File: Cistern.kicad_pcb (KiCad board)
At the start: 2 copper layers, 51 x 83 mm, 14 parts, among them J2 Gauge Stepper, J3 Power Connector, Q1 IRF9540N, SW1 WiFi reset switch, SW2 Water Sensor, U1 ULN2003A, U3 Boost Converter (5->20 V)

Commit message: Changing schematic to fit parts and starting PCB design
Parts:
- D1: footprint LED_THT:LED_D4.0mm -> LED_THT:LED_D5.0mm
- Q1: value IRF9540N -> BD244C
- R1: value 250 -> 150
- R2: value 200k -> 68
- R4: value 160 -> 150
- moved SW1 85.8 mm to (112.5, 22.6), turned to 180 degrees
- moved U3 63.6 mm to (76.2, 99.1)
- moved J2 56.8 mm to (63.5, 94.0), turned to 180 degrees
- moved U1 36.4 mm to (66.0, 78.7), turned to -90 degrees
- moved R2 32.6 mm to (71.1, 96.5), turned to 90 degrees
- moved D2 26.4 mm to (88.9, 48.3), turned to -90 degrees
- moved D1 22.1 mm to (33.0, 88.9)
- moved Q1 19.1 mm to (71.1, 78.7), turned to -90 degrees
- moved D3 18.1 mm to (81.3, 48.3), turned to 180 degrees
- moved R1 14.3 mm to (81.3, 53.3), turned to 180 degrees
- moved J3 13.7 mm to (88.9, 38.1), turned to -90 degrees
- moved R4 2.39 mm to (45.7, 91.4), turned to -90 degrees
- moved SW2 1.30 mm to (88.9, 27.9), turned to -90 degrees
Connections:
- Q1 pad 1: Net-(Q1-G) -> Net-(Q1-B)
- R2 pad 1: +5V -> Net-(Q1-B)
- R2 pad 2: Net-(Q1-G) -> Net-(U1-O1)
- U1 pad 1: Net-(MCU1-GPIO27) -> Net-(MCU1-GPIO35)
- U1 pad 10: Net-(D1-K) -> unconnected-(U1-O7-Pad10)
- U1 pad 11: Net-(Q1-G) -> Net-(D1-K)
- U1 pad 12: unconnected-(U1-O5-Pad12) -> Net-(J2-Pin_4)
- U1 pad 13: Net-(J2-Pin_4) -> Net-(J2-Pin_3)
- U1 pad 14: Net-(J2-Pin_3) -> Net-(J2-Pin_2)
- U1 pad 15: Net-(J2-Pin_2) -> Net-(J2-Pin_1)
- U1 pad 16: Net-(J2-Pin_1) -> Net-(U1-O1)
- U1 pad 2: Net-(MCU1-GPIO26) -> Net-(MCU1-GPIO32)
- U1 pad 3: Net-(MCU1-GPIO25) -> Net-(MCU1-GPIO33)
- U1 pad 4: Net-(MCU1-GPIO33) -> Net-(MCU1-GPIO25)
- U1 pad 5: unconnected-(U1-I5-Pad5) -> Net-(MCU1-GPIO26)
- U1 pad 6: Net-(MCU1-GPIO32) -> Net-(MCU1-GPIO27)
- U1 pad 7: Net-(MCU1-GPIO35) -> unconnected-(U1-I7-Pad7)
- U1 pad 9: GND -> +5V
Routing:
- net GND: track 0.00 -> 114.3 mm
- net Net-(MCU1-GPIO15): track 0.00 -> 43.2 mm
- net +5V: track 0.00 -> 25.4 mm
- net Net-(MCU1-GPIO4): track 0.00 -> 20.3 mm
- net Net-(D2-A): track 0.00 -> 18.0 mm
- net Net-(D2-K): track 0.00 -> 12.7 mm
- removed copper zone on B.Cu, net (none)
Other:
- board size 51 x 83 mm -> 55.5 x 79.6 mm

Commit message: Working on board layout
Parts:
- added BZ1: Buzzer, Cistern:AZDelivery_KY-012_Buzzer, F.Cu at (48.3, 78.7)
- D2, SW2: footprint TerminalBlock:TerminalBlock_bornier-2_P5.08mm -> Connector_PinHeader_2.54mm:PinHeader_1x02_P2.54mm_Vertical
- moved SW1 80.0 mm to (43.8, 63.5), turned to 90 degrees
- moved J3 74.7 mm to (45.7, 99.1), turned to 0 degrees
- moved D2 52.4 mm to (68.6, 96.5), turned to 90 degrees
- moved D3 48.8 mm to (50.8, 86.4)
- moved R1 48.8 mm to (50.8, 91.4)
- moved U3 43.8 mm to (94.0, 59.1), turned to -90 degrees
- moved MCU1 27.0 mm to (48.3, 50.8), turned to 90 degrees
- moved SW2 25.5 mm to (91.4, 53.3)
- moved D1 25.5 mm to (58.4, 86.4)
- moved J2 23.4 mm to (68.6, 71.1)
- moved U1 23.4 mm to (71.1, 55.9)
- moved Q1 13.7 mm to (66.0, 91.4), turned to 90 degrees
- moved R4 12.7 mm to (53.3, 81.3), turned to 90 degrees
- moved R2 5.08 mm to (71.1, 91.4)
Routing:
- net +5V: track 25.4 -> 129.5 mm
- net Net-(Q1-C): track 0.00 -> 57.8 mm
- net Net-(BZ1--): track 0.00 -> 20.3 mm
- net Net-(U1-O1): track 0.00 -> 20.3 mm
- net GND: track 114.3 -> 129.4 mm
- net Net-(MCU1-GPIO4): track 20.3 -> 6.50 mm
- net Net-(D2-K): track 12.7 -> 22.9 mm
- net Net-(J2-Pin_4): track 0.00 -> 7.62 mm
- net Net-(J2-Pin_3): track 0.00 -> 7.62 mm
- net Net-(J2-Pin_2): track 0.00 -> 7.62 mm
- net Net-(J2-Pin_1): track 0.00 -> 7.62 mm
- net Net-(D2-A): track 18.0 -> 25.4 mm
- net Net-(Q1-B): track 0.00 -> 5.08 mm
- net Net-(MCU1-GPIO15): track 43.2 -> 40.6 mm

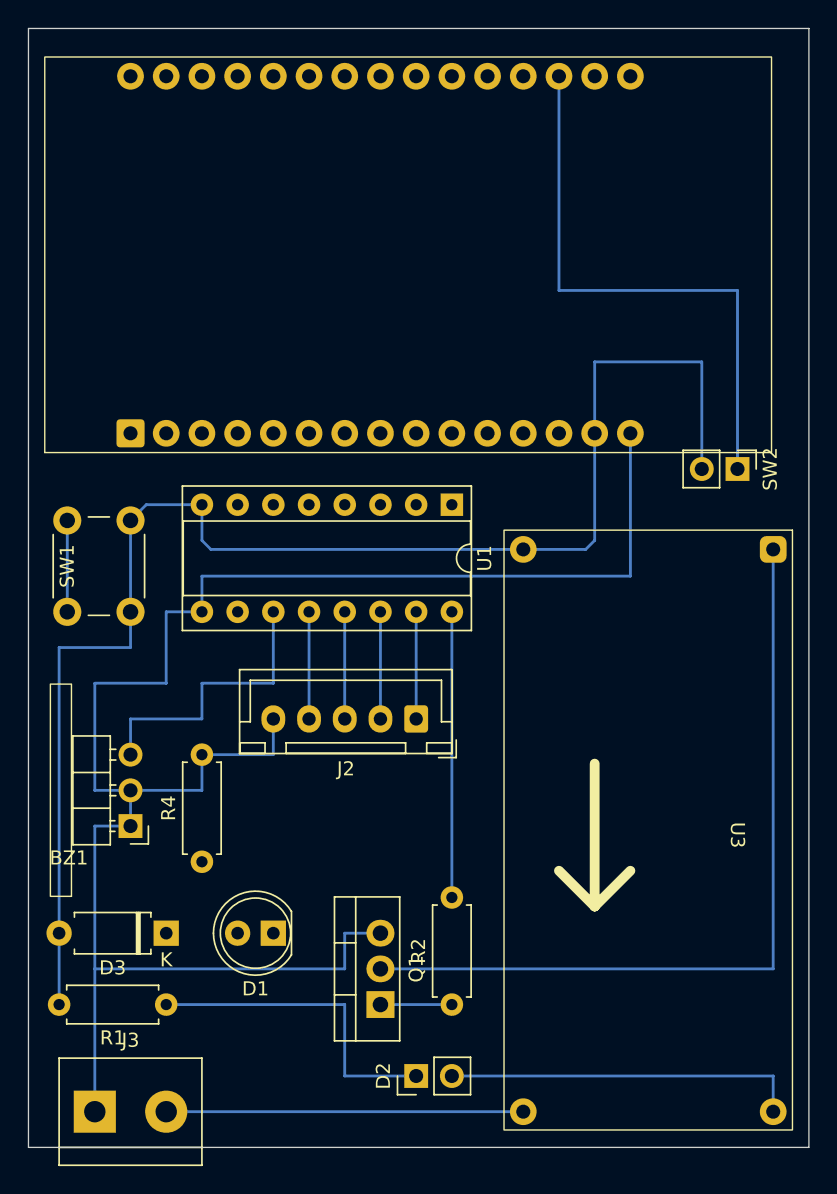
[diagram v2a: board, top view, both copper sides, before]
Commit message: Finishing hole-grid ready PCB design
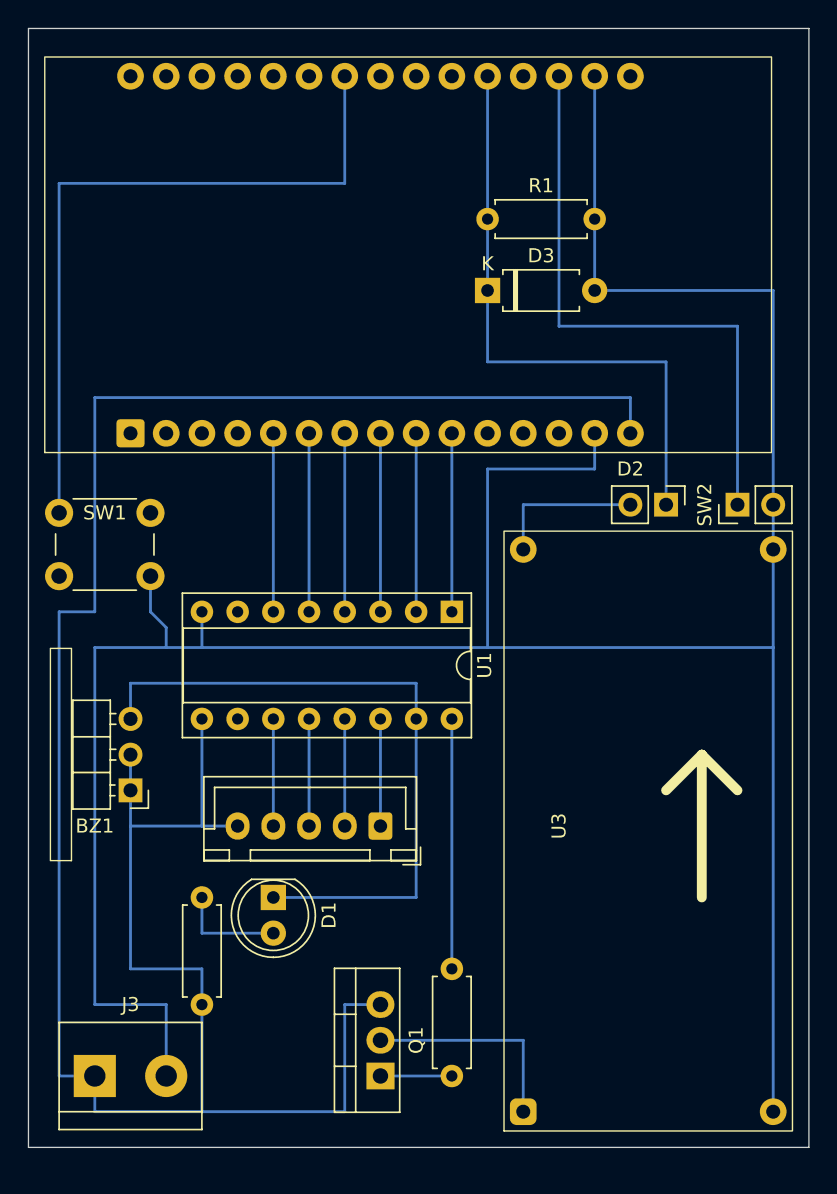
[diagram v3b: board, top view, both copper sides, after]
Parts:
- SW1: value WiFi reset switch -> WiFi reset
- moved R1 60.4 mm to (73.7, 35.6), turned to 0 degrees
- moved D3 51.1 mm to (73.7, 40.6), turned to 0 degrees
- moved D2 44.4 mm to (86.4, 55.9), turned to -90 degrees
- moved U3 43.8 mm to (76.2, 99.1), turned to 90 degrees
- moved J2 8.03 mm to (66.0, 78.7)
- moved U1 7.62 mm to (71.1, 63.5)
- moved SW1 7.06 mm to (43.2, 56.5), turned to 0 degrees
- moved Q1 5.08 mm to (66.0, 96.5)
- moved R2 5.08 mm to (71.1, 96.5)
- moved D1 2.54 mm to (58.4, 83.8), turned to -90 degrees
- moved J3 2.54 mm to (45.7, 96.5)
- moved SW2 2.54 mm to (91.4, 55.9), turned to 90 degrees
- moved BZ1 2.54 mm to (48.3, 76.2)
- moved R4 2.54 mm to (53.3, 83.8), turned to -90 degrees
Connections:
- MCU1 pad 22: Net-(D2-K) -> Net-(MCU1-GPIO18)
- MCU1 pad 26: Net-(MCU1-GPIO4) -> Net-(D2-K)
- SW1 pad 1: Net-(MCU1-GPIO4) -> Net-(MCU1-GPIO18)
- U1 pad 1: Net-(MCU1-GPIO35) -> Net-(MCU1-GPIO27)
- U1 pad 11: Net-(BZ1--) -> Net-(J2-Pin_4)
- U1 pad 12: Net-(J2-Pin_4) -> Net-(J2-Pin_3)
- U1 pad 13: Net-(J2-Pin_3) -> Net-(J2-Pin_2)
- U1 pad 14: Net-(J2-Pin_2) -> Net-(J2-Pin_1)
- U1 pad 15: Net-(J2-Pin_1) -> Net-(BZ1--)
- U1 pad 2: Net-(MCU1-GPIO32) -> Net-(MCU1-GPIO26)
- U1 pad 3: Net-(MCU1-GPIO33) -> Net-(MCU1-GPIO25)
- U1 pad 4: Net-(MCU1-GPIO25) -> Net-(MCU1-GPIO33)
- U1 pad 5: Net-(MCU1-GPIO26) -> Net-(MCU1-GPIO32)
- U1 pad 6: Net-(MCU1-GPIO27) -> Net-(MCU1-GPIO35)
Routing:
- net GND: track 129.4 -> 201.1 mm
- net Net-(MCU1-GPIO18): track 0.00 -> 51.4 mm
- net Net-(Q1-C): track 57.8 -> 15.2 mm
- net +5V: track 129.5 -> 170.2 mm
- net Net-(BZ1--): track 20.3 -> 48.3 mm
- net Net-(D2-K): track 22.9 -> 43.2 mm
- net Net-(D2-A): track 25.4 -> 10.8 mm
- net Net-(MCU1-GPIO35): track 0.00 -> 12.7 mm
- net Net-(MCU1-GPIO33): track 0.00 -> 12.7 mm
- net Net-(MCU1-GPIO32): track 0.00 -> 12.7 mm
- net Net-(MCU1-GPIO27): track 0.00 -> 12.7 mm
- net Net-(MCU1-GPIO26): track 0.00 -> 12.7 mm
- net Net-(MCU1-GPIO25): track 0.00 -> 12.7 mm
- net Net-(D1-A): track 0.00 -> 7.62 mm
- net Net-(MCU1-GPIO4): track 6.50 -> 0.00 mm
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
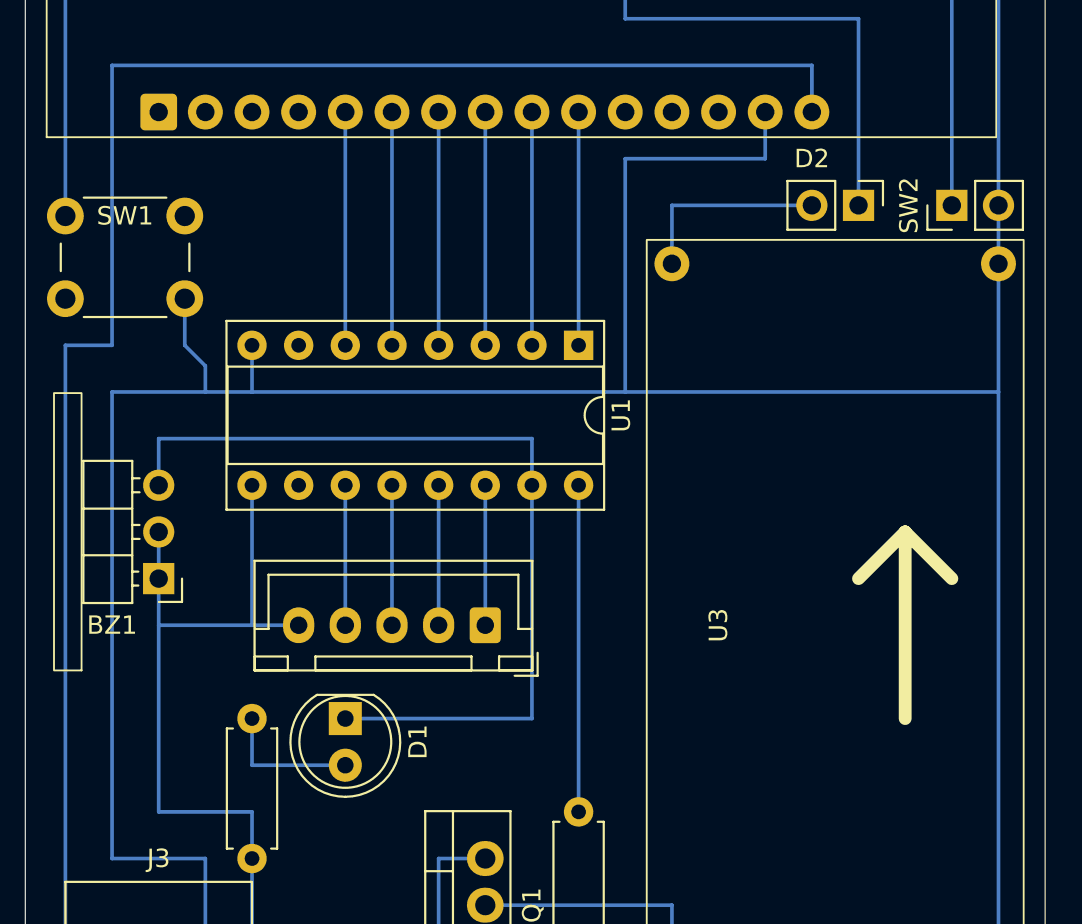
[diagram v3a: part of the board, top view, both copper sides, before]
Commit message: Small improvement to buzzer clearance
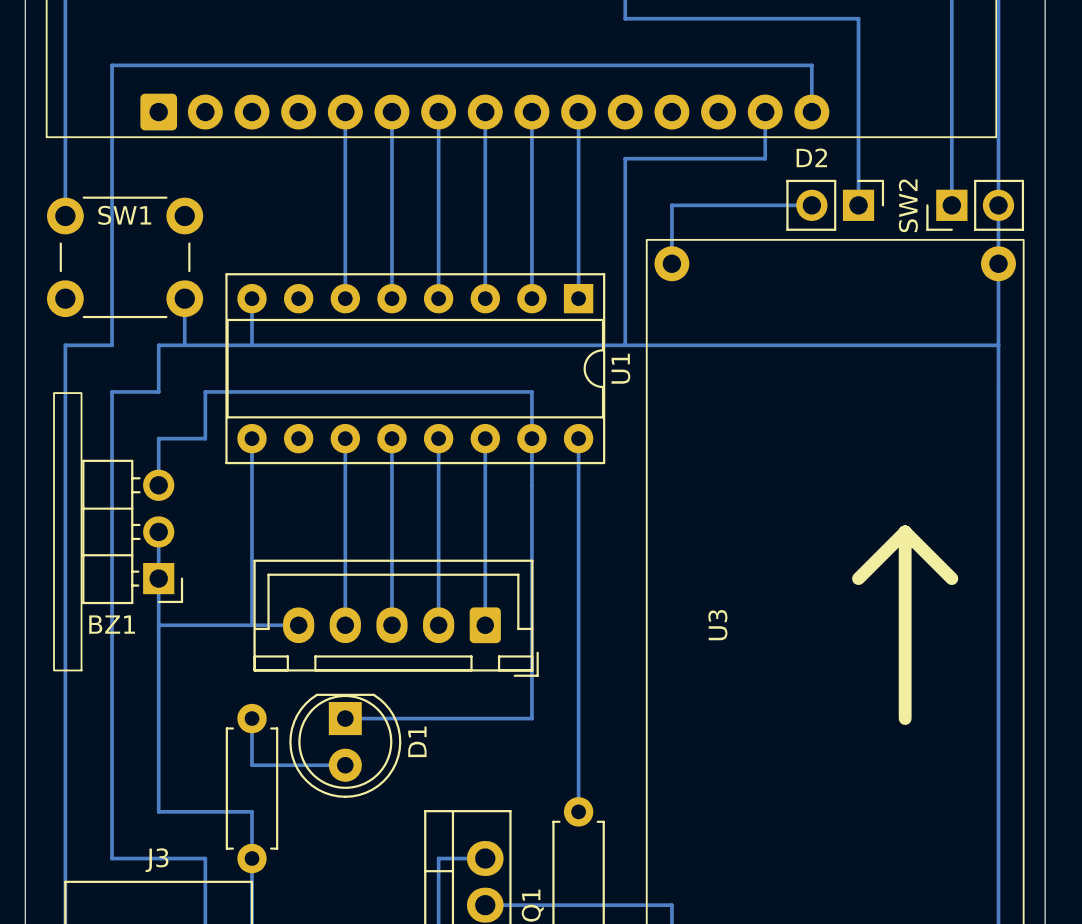
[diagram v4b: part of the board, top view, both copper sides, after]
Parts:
- moved U1 2.54 mm to (71.1, 61.0)
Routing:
- net Net-(BZ1--): track 48.3 -> 53.3 mm
- net GND: track 201.1 -> 198.1 mm
- net Net-(U1-O1): track 17.8 -> 20.3 mm
- net Net-(J2-Pin_4): track 7.62 -> 10.2 mm
- net Net-(J2-Pin_3): track 7.62 -> 10.2 mm
- net Net-(J2-Pin_2): track 7.62 -> 10.2 mm
- net Net-(J2-Pin_1): track 7.62 -> 10.2 mm
- net Net-(MCU1-GPIO35): track 12.7 -> 10.2 mm
- net Net-(MCU1-GPIO33): track 12.7 -> 10.2 mm
- net Net-(MCU1-GPIO32): track 12.7 -> 10.2 mm
- net Net-(MCU1-GPIO27): track 12.7 -> 10.2 mm
- net Net-(MCU1-GPIO26): track 12.7 -> 10.2 mm
- net Net-(MCU1-GPIO25): track 12.7 -> 10.2 mm
- net +5V: track 170.2 -> 172.7 mm
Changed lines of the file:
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@@
 		)
 		(fp_text user "${REFERENCE}"
-			(at 0 1.27 360)
+			(at 0 1.27 0)
 			(layer "F.Fab")
 			(effects
@@
 		(tags "Diode A-405 series Axial Horizontal pin pitch 7.62mm  length 5.2mm diameter 2.7mm")
 		(property "Reference" "D3"
-			(at 3.81 -2.47 360)
+			(at 3.81 -2.47 0)
 			(layer "F.SilkS")
 			(effects
@@
 		)
 		(property "Value" "3V"
-			(at 3.81 2.47 360)
+			(at 3.81 2.47 0)
 			(layer "F.Fab")
 			(effects
@@
 		)
 		(fp_text user "K"
-			(at 0 -1.9 360)
+			(at 0 -1.9 0)
 			(layer "F.SilkS")
 			(effects
@@
 		)
 		(fp_text user "${REFERENCE}"
-			(at 4.2 0 360)
+			(at 4.2 0 0)
 			(layer "F.Fab")
 			(effects
@@
 		)
 		(fp_text user "K"
-			(at 0 -1.9 360)
+			(at 0 -1.9 0)
 			(layer "F.Fab")
 			(effects
@@
 		)
 		(fp_text user "${REFERENCE}"
-			(at 0 1.27 360)
+			(at 0 1.27 0)
 			(layer "F.Fab")
 			(effects
@@
 		(tags "Resistor Axial_DIN0207 series Axial Horizontal pin pitch 7.62mm 0.25W = 1/4W length 6.3mm diameter 2.5mm")
 		(property "Reference" "R1"
-			(at 3.81 -2.37 360)
+			(at 3.81 -2.37 0)
 			(layer "F.SilkS")
 			(effects
@@
 		)
 		(property "Value" "150"
-			(at 3.81 2.37 360)
+			(at 3.81 2.37 0)
 			(layer "F.Fab")
 			(effects
@@
 		)
 		(fp_text user "${REFERENCE}"
-			(at 3.81 0 360)
+			(at 3.81 0 0)
 			(layer "F.Fab")
 			(effects
@@
 		(tags "terminal block bornier2")
 		(property "Reference" "J3"
-			(at 2.54 -5.08 360)
+			(at 2.54 -5.08 0)
 			(layer "F.SilkS")
 			(effects
@@
 		)
 		(property "Value" "Power Connector"
-			(at 2.54 3.81 360)
+			(at 2.54 3.81 0)
 			(layer "F.Fab")
 			(effects
@@
 		)
 		(fp_text user "${REFERENCE}"
-			(at 2.54 0 360)
+			(at 2.54 0 0)
 			(layer "F.Fab")
 			(effects
@@
 		(tags "tact sw push 6mm")
 		(property "Reference" "SW1"
-			(at 3.25 0 360)
+			(at 3.25 0 0)
 			(layer "F.SilkS")
 			(effects
@@
 		)
 		(fp_text user "${REFERENCE}"
-			(at 3.25 2.25 360)
+			(at 3.25 2.25 0)
 			(layer "F.Fab")
 			(effects
@@
 	(footprint "Package_DIP:DIP-16_W7.62mm_Socket"
 		(layer "F.Cu")
-		(at 71.12 63.5 -90)
+		(at 71.12 60.96 -90)
 		(descr "16-lead though-hole mounted DIP package, row spacing 7.62 mm (300 mils), Socket")
 		(tags "THT DIP DIL PDIP 2.54mm 7.62mm 300mil Socket")
@@
 	)
 	(segment
-		(start 53.34 78.74)
-		(end 53.34 71.12)
-		(width 0.2)
-		(layer "B.Cu")
-		(net 1)
-	)
-	(segment
 		(start 45.72 63.5)
 		(end 45.72 48.26)
@@
 	)
 	(segment
+		(start 53.34 68.58)
+		(end 53.34 78.74)
+		(width 0.2)
+		(layer "B.Cu")
+		(net 1)
+	)
+	(segment
 		(start 43.18 63.5)
 		(end 45.72 63.5)
@@
 	)
 	(segment
+		(start 50.8 66.04)
+		(end 68.58 66.04)
+		(width 0.2)
+		(layer "B.Cu")
+		(net 2)
+	)
+	(segment
 		(start 68.58 68.58)
 		(end 68.58 71.12)
@@
 	)
 	(segment
+		(start 68.58 66.04)
+		(end 68.58 68.58)
+		(width 0.2)
+		(layer "B.Cu")
+		(net 2)
+	)
+	(segment
 		(start 58.42 83.82)
 		(end 68.58 83.82)
@@
 	)
 	(segment
+		(start 50.8 68.58)
+		(end 50.8 66.04)
+		(width 0.2)
+		(layer "B.Cu")
+		(net 2)
+	)
+	(segment
 		(start 48.26 71.12)
 		(end 48.26 68.58)
@@
 	(segment
 		(start 48.26 68.58)
-		(end 68.58 68.58)
+		(end 50.8 68.58)
 		(width 0.2)
 		(layer "B.Cu")
@@
 	)
 	(segment
-		(start 50.8 66.04)
-		(end 53.34 66.04)
+		(start 50.8 91.44)
+		(end 45.72 91.44)
+		(width 0.2)
+		(layer "B.Cu")
+		(net 6)
+	)
+	(segment
+		(start 73.66 53.34)
+		(end 81.28 53.34)
+		(width 0.2)
+		(layer "B.Cu")
+		(net 6)
+	)
+	(segment
+		(start 81.28 53.34)
+		(end 81.28 50.8)
 		(width 0.2)
 		(layer "B.Cu")
@@
 	(segment
 		(start 53.34 63.5)
-		(end 53.34 66.04)
+		(end 73.66 63.5)
 		(width 0.2)
 		(layer "B.Cu")
@@
 	)
 	(segment
-		(start 50.8 91.44)
-		(end 45.72 91.44)
+		(start 49.68 63.5)
+		(end 53.34 63.5)
 		(width 0.2)
 		(layer "B.Cu")
@@
 	)
 	(segment
-		(start 73.66 53.34)
-		(end 81.28 53.34)
+		(start 48.26 66.04)
+		(end 48.26 63.5)
 		(width 0.2)
 		(layer "B.Cu")
@@
 	)
 	(segment
-		(start 81.28 53.34)
-		(end 81.28 50.8)
+		(start 45.72 66.04)
+		(end 48.26 66.04)
 		(width 0.2)
 		(layer "B.Cu")
@@
 	)
 	(segment
-		(start 73.66 66.04)
-		(end 73.66 53.34)
+		(start 93.98 63.5)
+		(end 93.98 59.06)
 		(width 0.2)
 		(layer "B.Cu")
@@
 	)
 	(segment
-		(start 53.34 66.04)
-		(end 73.66 66.04)
+		(start 73.66 63.5)
+		(end 93.98 63.5)
 		(width 0.2)
 		(layer "B.Cu")
@@
 	)
 	(segment
-		(start 49.68 63.5)
-		(end 50.8 64.62)
+		(start 48.26 63.5)
+		(end 49.68 63.5)
 		(width 0.2)
 		(layer "B.Cu")
@@
 	)
 	(segment
-		(start 73.66 66.04)
-		(end 93.98 66.04)
+		(start 93.98 66.04)
+		(end 93.98 63.5)
 		(width 0.2)
 		(layer "B.Cu")
@@
 	)
 	(segment
-		(start 93.98 99.06)
-		(end 93.98 66.04)
+		(start 53.34 60.96)
+		(end 53.34 63.5)
 		(width 0.2)
 		(layer "B.Cu")
@@
 	)
 	(segment
-		(start 81.28 40.64)
-		(end 93.98 40.64)
+		(start 93.98 99.06)
+		(end 93.98 66.04)
 		(width 0.2)
 		(layer "B.Cu")
@@
 	)
 	(segment
-		(start 45.72 66.04)
-		(end 50.8 66.04)
+		(start 73.66 63.5)
+		(end 73.66 53.34)
 		(width 0.2)
 		(layer "B.Cu")
@@
 	)
 	(segment
-		(start 50.8 64.62)
-		(end 50.8 66.04)
+		(start 81.28 40.64)
+		(end 93.98 40.64)
 		(width 0.2)
 		(layer "B.Cu")
@@
 	)
 	(segment
-		(start 93.98 66.04)
-		(end 93.98 59.06)
-		(width 0.2)
-		(layer "B.Cu")
-		(net 6)
-	)
-	(segment
-		(start 58.42 71.12)
+		(start 58.42 68.58)
 		(end 58.42 78.74)
 		(width 0.2)
@@
 	)
 	(segment
-		(start 66.04 71.12)
+		(start 66.04 68.58)
 		(end 66.04 78.74)
 		(width 0.2)
@@
 	)
 	(segment
-		(start 60.96 71.12)
+		(start 60.96 68.58)
 		(end 60.96 78.74)
 		(width 0.2)
@@
 	)
 	(segment
-		(start 63.5 71.12)
+		(start 63.5 68.58)
 		(end 63.5 78.74)
 		(width 0.2)
@@
 	(segment
 		(start 68.58 50.8)
-		(end 68.58 63.5)
+		(end 68.58 60.96)
 		(width 0.2)
 		(layer "B.Cu")
@@
 	(segment
 		(start 63.5 50.8)
-		(end 63.5 63.5)
+		(end 63.5 60.96)
 		(width 0.2)
 		(layer "B.Cu")
@@
 	(segment
 		(start 58.42 50.8)
-		(end 58.42 63.5)
+		(end 58.42 60.96)
 		(width 0.2)
 		(layer "B.Cu")
@@
 	(segment
 		(start 71.12 50.8)
-		(end 71.12 63.5)
+		(end 71.12 60.96)
 		(width 0.2)
 		(layer "B.Cu")
@@
 	(segment
 		(start 60.96 50.8)
-		(end 60.96 63.5)
+		(end 60.96 60.96)
 		(width 0.2)
 		(layer "B.Cu")
@@
 	(segment
 		(start 66.04 50.8)
-		(end 66.04 63.5)
+		(end 66.04 60.96)
 		(width 0.2)
 		(layer "B.Cu")
@@
 	)
 	(segment
-		(start 71.12 88.9)
-		(end 71.12 71.12)
+		(start 71.12 68.58)
+		(end 71.12 88.9)
 		(width 0.2)
 		(layer "B.Cu")
